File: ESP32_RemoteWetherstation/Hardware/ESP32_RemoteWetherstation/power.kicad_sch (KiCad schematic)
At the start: 5 parts, among them IC301 TLV77333PDBVR

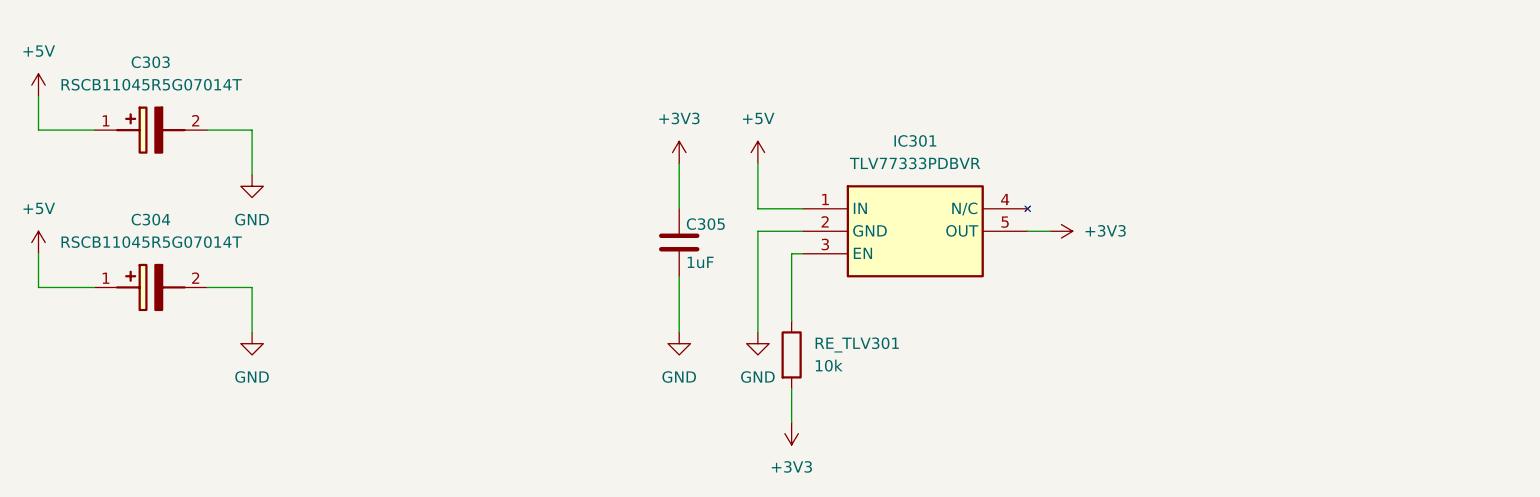
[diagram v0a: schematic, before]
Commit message: added IO, changed LDO
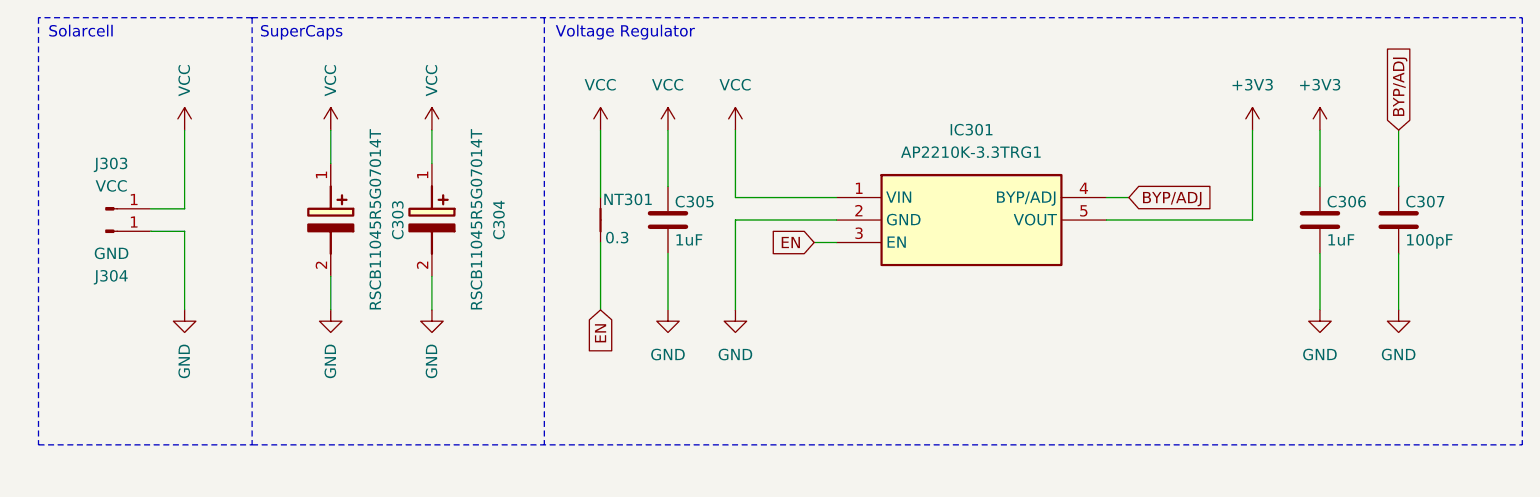
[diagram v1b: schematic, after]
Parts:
- removed IC301: TLV77333PDBVR, TLV77333PDBVR:SOT95P280X145-5N, symbol TLV77333PDBVR:TLV77333PDBVR
- removed RE_TLV301: 10k, Resistor_SMD:R_0603_1608Metric, symbol Device:R
- added C306: 1uF, Capacitor_SMD:C_0805_2012Metric_Pad1.18x1.45mm_HandSolder, symbol Device:C
- added C307: 100pF, Capacitor_SMD:C_0603_1608Metric_Pad1.08x0.95mm_HandSolder, symbol Device:C
- added IC301: AP2210K-3.3TRG1, LibKiCad:SOT95P282X145-5N, symbol SamacSys_Parts:AP2210K-3.3TRG1
- added J303: VCC, Connector_Wire:SolderWire-0.75sqmm_1x01_D1.25mm_OD2.3mm, symbol Connector:Conn_01x01_Pin
- added J304: GND, Connector_Wire:SolderWire-0.75sqmm_1x01_D1.25mm_OD2.3mm, symbol Connector:Conn_01x01_Pin
- added NT301: 0.3, Nettie_Jan:NetTie-2_SMD_Pad0.3mm, symbol Device:NetTie_2
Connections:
- net +3V3: now also C306.1, IC301.5 (VOUT); no longer C305.1
- net GND: now also C306.2, C307.2, IC301.2 (GND), J304.1 (Pin_1)
- net +5V renamed VCC
- net VCC: now also C305.1, IC301.1 (VIN), J303.1 (Pin_1), NT301.2
- new net BYP/ADJ: C307.1, IC301.4 (BYP/ADJ)
- new net EN: IC301.3 (EN), NT301.1
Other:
- note added: "Solarcell"
- note added: "SuperCaps"
- note added: "Voltage Regulator"
- moved on the sheet: C304

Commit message: Stitching/power module (#7)
* test: gitpush

* edited schematic looks

* deleted Backups

* StitchingPCB/try1
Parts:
- C307: footprint Capacitor_SMD:C_0603_1608Metric_Pad1.08x0.95mm_HandSolder -> Capacitor_SMD:C_0402_1005Metric
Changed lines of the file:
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@@
 			)
 		)
-		(property "Footprint" "Capacitor_SMD:C_0603_1608Metric_Pad1.08x0.95mm_HandSolder"
+		(property "Footprint" "Capacitor_SMD:C_0402_1005Metric"
 			(at 195.2752 66.04 0)
 			(effects

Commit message: Connected IO
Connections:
- net GND: no longer J304.1 (Pin_1)
- new net GND1: J304.1 (Pin_1)
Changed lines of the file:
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@@
+	)
+	(symbol
+		(lib_id "power:GND1")
+		(at 57.15 72.39 0)
+		(unit 1)
+		(exclude_from_sim no)
+		(in_bom yes)
+		(on_board yes)
+		(dnp no)
+		(fields_autoplaced yes)
+		(property "Reference" "#PWR0603"
+			(at 57.15 78.74 0)
+			(effects
+				(font
+					(size 1.27 1.27)
+				)
+				(hide yes)
+			)
+		)
+		(property "Value" "GND1"
+			(at 57.15 77.47 0)
+			(effects
+				(font
+					(size 1.27 1.27)
+				)
+			)
+		)
+		(property "Footprint" ""
+			(at 57.15 72.39 0)
+			(effects
+				(font
+					(size 1.27 1.27)
+				)
+				(hide yes)
+			)
+		)
+		(property "Datasheet" ""
+			(at 57.15 72.39 0)
+			(effects
+				(font
+					(size 1.27 1.27)
+				)
+				(hide yes)
+			)
+		)
+		(property "Description" "Power symbol creates a global label with name \"GND1\" , ground"
+			(at 57.15 72.39 0)
+			(effects
+				(font
+					(size 1.27 1.27)
+				)
+				(hide yes)
+			)
+		)
+		(pin "1"
+		)
+		(instances
+			(project ""
+				(path "/bb194ab9-ddae-46dd-ae5d-1e0c862ad374/884b25f4-a511-4e9d-bd1d-34e166fc4cfd"
+					(reference "#PWR0603")
+					(unit 1)
+				)
+			)
+		)
 	)
 	(symbol
@@
 					(unit 1)
 				)
-			)
-		)
-	)
-	(symbol
-		(lib_id "power:GND")
-		(at 57.15 72.39 0)
-		(unit 1)
-		(exclude_from_sim no)
-		(in_bom yes)
-		(on_board yes)
-		(dnp no)
-		(fields_autoplaced yes)
-		(property "Reference" "#PWR0323"
-			(at 57.15 78.74 0)
-			(effects
-				(font
-					(size 1.27 1.27)
-				)
-				(hide yes)
-			)
-		)
-		(property "Value" "GND"
-			(at 57.1501 76.2 90)
-			(effects
-				(font
-					(size 1.27 1.27)
-				)
-				(justify right)
-			)
-		)
-		(property "Footprint" ""
-			(at 57.15 72.39 0)
-			(effects
-				(font
-					(size 1.27 1.27)
-				)
-				(hide yes)
-			)
-		)
-		(property "Datasheet" ""
-			(at 57.15 72.39 0)
-			(effects
-				(font
-					(size 1.27 1.27)
-				)
-				(hide yes)
-			)
-		)
-		(property "Description" "Power symbol creates a global label with name \"GND\" , ground"
-			(at 57.15 72.39 0)
-			(effects
-				(font
-					(size 1.27 1.27)
-				)
-				(hide yes)
-			)
-		)
-		(pin "1"
-		)
-		(instances
-			(project "ESP32_RemoteWetherstation"
-				(path "/bb194ab9-ddae-46dd-ae5d-1e0c862ad374/884b25f4-a511-4e9d-bd1d-34e166fc4cfd"
-					(reference "#PWR0323")
-					(unit 1)
-				)
